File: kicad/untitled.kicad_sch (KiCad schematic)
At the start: 3 parts, among them J2 NMJ4HCD2, J3 AudioJack3_Dual_Switch, J4 Conn_01x03_Pin

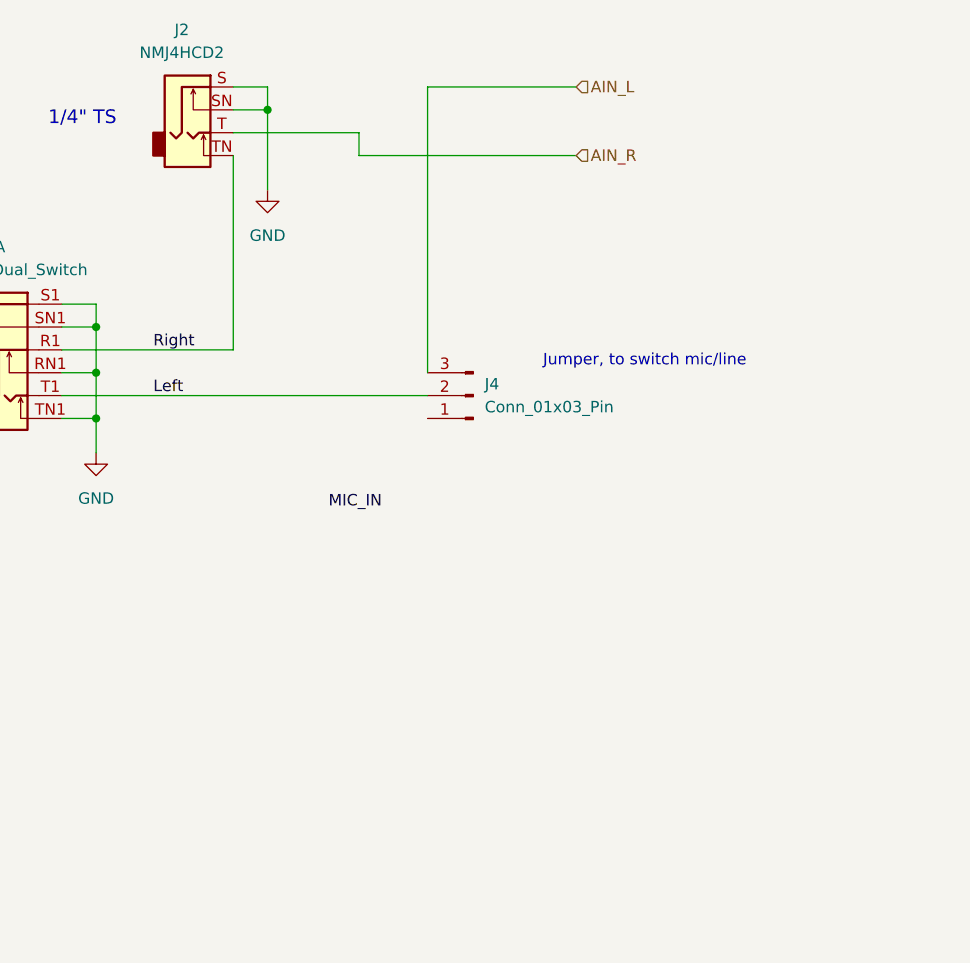
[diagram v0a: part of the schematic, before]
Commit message: microphone preamp. May give up on the jumper idea and add another jack
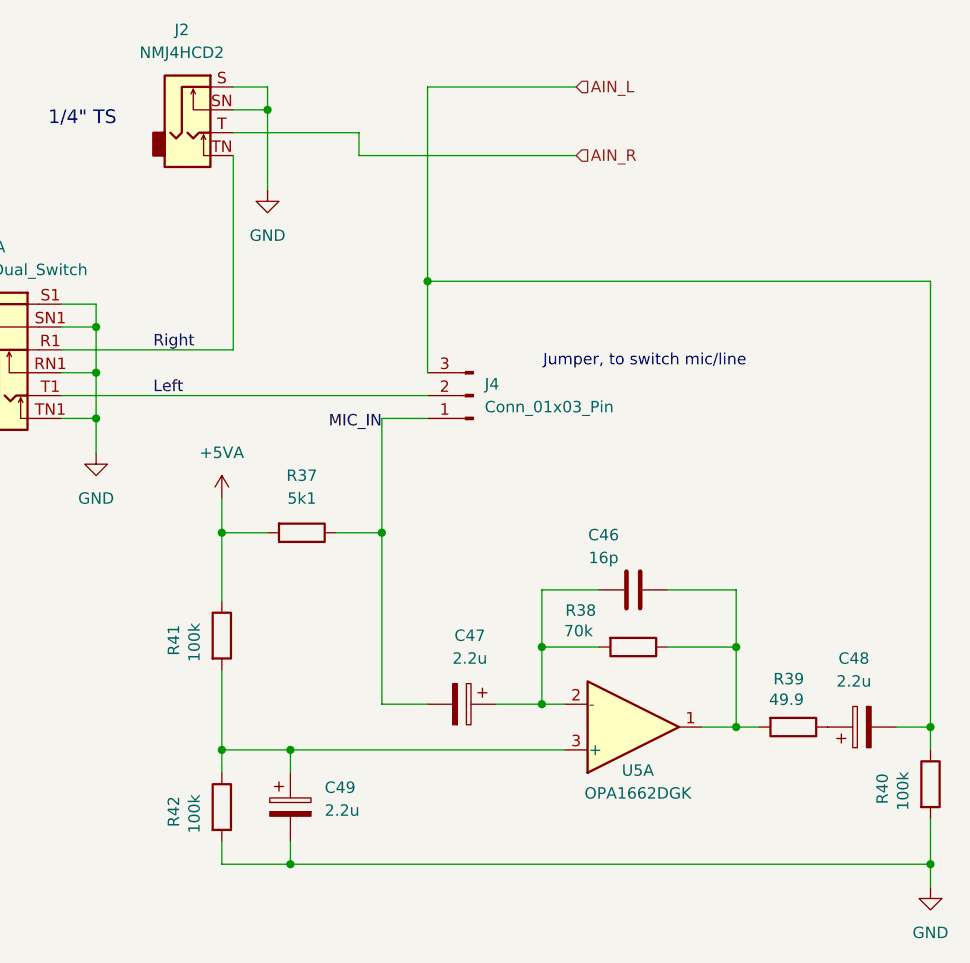
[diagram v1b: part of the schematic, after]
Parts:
- added C46: 16p, symbol Device:C
- added C47, C48, C49: 2.2u, symbol Device:C_Polarized
- added R37: 5k1, symbol Device:R
- added R38: 70k, symbol Device:R
- added R39: 49.9, symbol Device:R
- added R40, R41, R42: 100k, symbol Device:R
- added U5: OPA1662DGK, Package_SO:VSSOP-8_3x3mm_P0.65mm, symbol Amplifier_Operational:OPA1662DGK
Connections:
- net AIN_L: now also C48.2, R40.1
- net GND: now also C49.2, R40.2, R42.2
- net MIC_IN: now also J4.1 (Pin_1), C47.2, R37.1
- new net: C48.1, R39.1
- new net: C46.2, R38.1, R39.2, U5.1
- new net: C49.1, R41.2, R42.1, U5.3 (+)
- new net: C46.1, C47.1, R38.2, U5.2 (-)
- new net +5VA: R37.2, R41.1

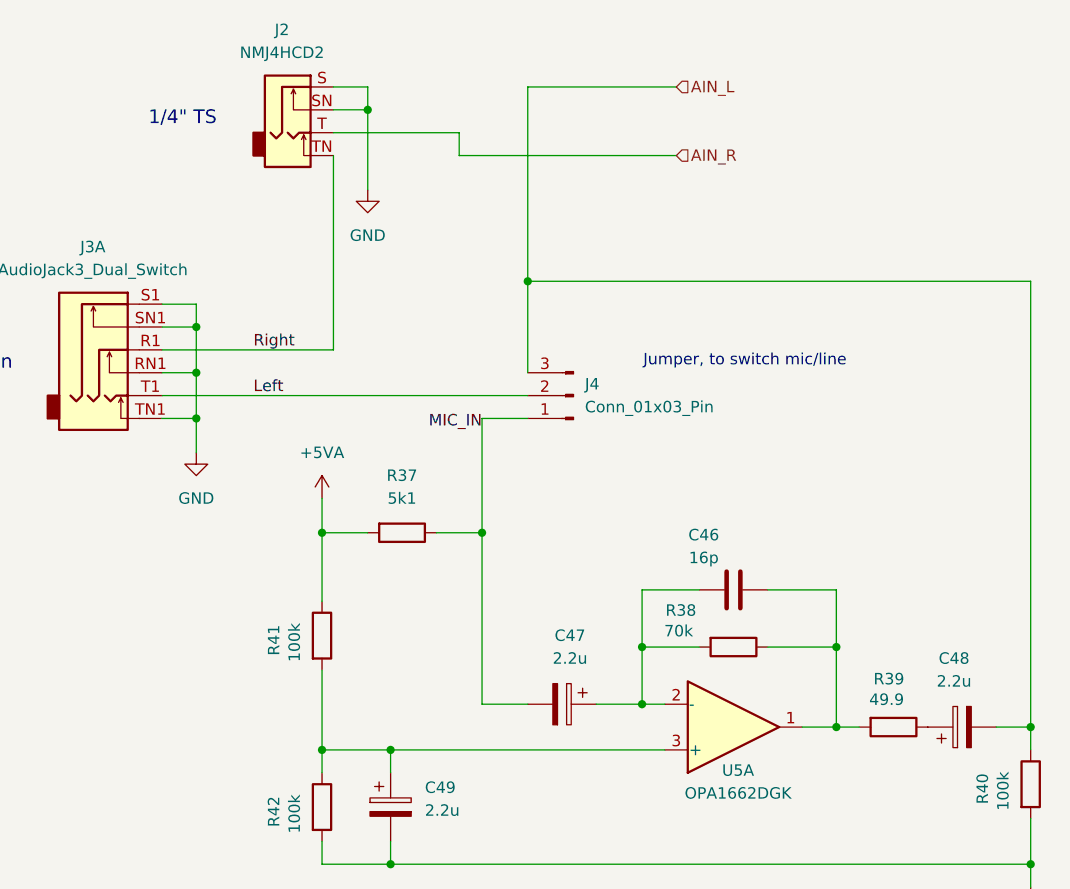
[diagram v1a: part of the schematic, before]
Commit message: DPDT switch for preamp toggle instead of jumper (not sure if this is a good solution)
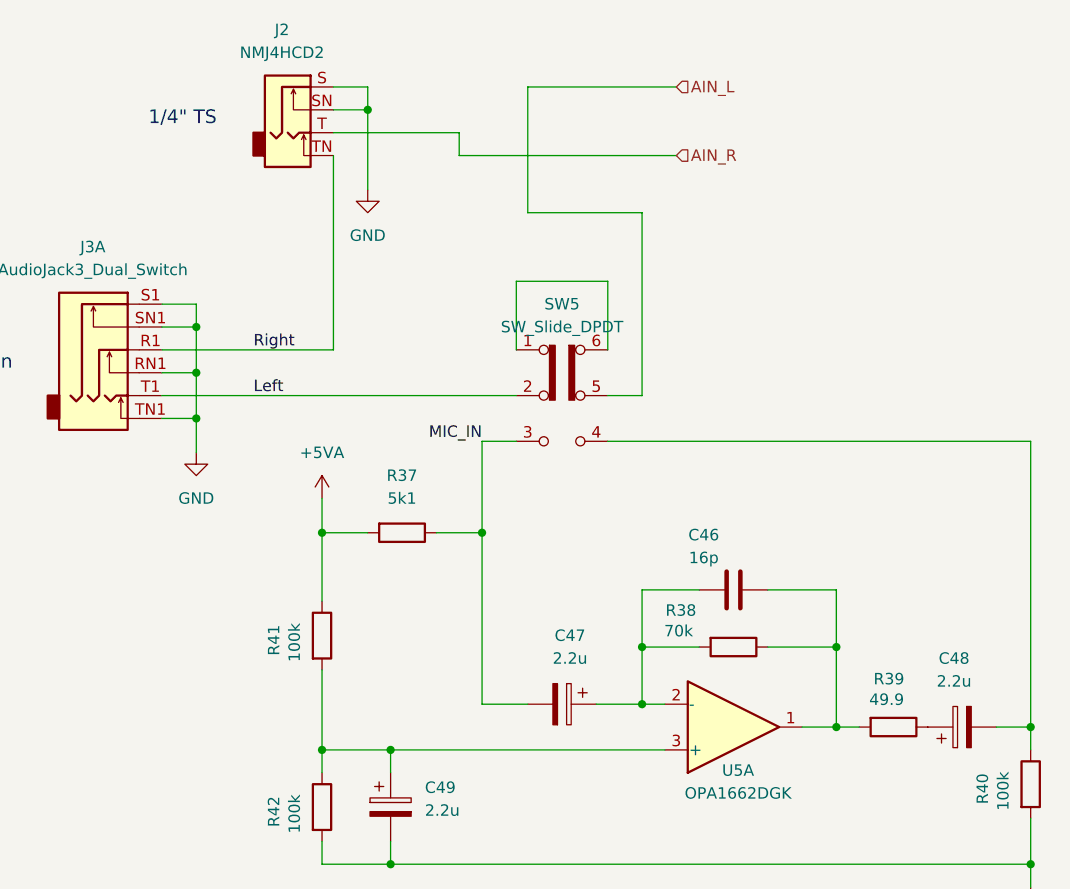
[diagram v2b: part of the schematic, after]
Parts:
- removed J4: Conn_01x03_Pin, symbol Connector:Conn_01x03_Pin
- added SW5: SW_Slide_DPDT, symbol Switch:SW_Slide_DPDT
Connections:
- net AIN_L: now also SW5.5 (B); no longer C48.2, R40.1
- net Left: now also SW5.2 (B)
- net MIC_IN: now also SW5.3 (C)
- new net: C48.2, R40.1, SW5.4 (A)
- new net: SW5.1 (A), SW5.6 (C)
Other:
- note removed: "Jumper, to switch mic/line"
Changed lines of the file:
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@@
-		)
-	)
-	(text "Jumper, to switch mic/line"
-		(exclude_from_sim no)
-		(at 120.65 106.68 0)
-		(effects
-			(font
-				(size 1.27 1.27)
-			)
 		)
 	)
@@
 	)
 	(junction
-		(at 152.4 147.32)
-		(diameter 0)
-		(color 0 0 0 0)
-	)
-	(junction
 		(at 109.22 144.78)
 		(diameter 0)
@@
 	)
 	(junction
-		(at 91.44 125.73)
+		(at 152.4 162.56)
 		(diameter 0)
 		(color 0 0 0 0)
 	)
 	(junction
-		(at 152.4 162.56)
+		(at 91.44 125.73)
 		(diameter 0)
 		(color 0 0 0 0)
@@
 	)
 	(junction
-		(at 96.52 97.79)
+		(at 152.4 147.32)
 		(diameter 0)
 		(color 0 0 0 0)
@@
 	(wire
 		(pts
+			(xy 95.25 105.41) (xy 95.25 97.79)
+		)
+		(stroke
+			(width 0)
+			(type default)
+		)
+	)
+	(wire
+		(pts
 			(xy 81.28 149.86) (xy 111.76 149.86)
 		)
@@
 	(wire
 		(pts
-			(xy 55.88 110.49) (xy 96.52 110.49)
+			(xy 95.25 115.57) (xy 91.44 115.57)
 		)
 		(stroke
@@
 	(wire
 		(pts
-			(xy 91.44 113.03) (xy 91.44 125.73)
-		)
-		(stroke
-			(width 0)
-			(type default)
-		)
-	)
-	(wire
-		(pts
 			(xy 73.66 162.56) (xy 73.66 160.02)
 		)
@@
 	(wire
 		(pts
+			(xy 109.22 90.17) (xy 96.52 90.17)
+		)
+		(stroke
+			(width 0)
+			(type default)
+		)
+	)
+	(wire
+		(pts
 			(xy 104.14 144.78) (xy 109.22 144.78)
 		)
@@
 	(wire
 		(pts
+			(xy 91.44 115.57) (xy 91.44 125.73)
+		)
+		(stroke
+			(width 0)
+			(type default)
+		)
+	)
+	(wire
+		(pts
 			(xy 74.93 76.2) (xy 78.74 76.2)
 		)
@@
 	(wire
 		(pts
+			(xy 105.41 110.49) (xy 109.22 110.49)
+		)
+		(stroke
+			(width 0)
+			(type default)
+		)
+	)
+	(wire
+		(pts
 			(xy 115.57 132.08) (xy 109.22 132.08)
 		)
@@
 	(wire
 		(pts
+			(xy 95.25 97.79) (xy 105.41 97.79)
+		)
+		(stroke
+			(width 0)
+			(type default)
+		)
+	)
+	(wire
+		(pts
 			(xy 55.88 100.33) (xy 59.69 100.33)
 		)
@@
 	(wire
 		(pts
+			(xy 152.4 115.57) (xy 152.4 147.32)
+		)
+		(stroke
+			(width 0)
+			(type default)
+		)
+	)
+	(wire
+		(pts
+			(xy 109.22 110.49) (xy 109.22 90.17)
+		)
+		(stroke
+			(width 0)
+			(type default)
+		)
+	)
+	(wire
+		(pts
 			(xy 59.69 113.03) (xy 59.69 116.84)
 		)
@@
 	(wire
 		(pts
-			(xy 96.52 97.79) (xy 152.4 97.79)
-		)
-		(stroke
-			(width 0)
-			(type default)
-		)
-	)
-	(wire
-		(pts
-			(xy 96.52 97.79) (xy 96.52 76.2)
+			(xy 96.52 90.17) (xy 96.52 76.2)
+		)
+		(stroke
+			(width 0)
+			(type default)
+		)
+	)
+	(wire
+		(pts
+			(xy 105.41 97.79) (xy 105.41 105.41)
 		)
 		(stroke
@@
 	(wire
 		(pts
-			(xy 96.52 107.95) (xy 96.52 97.79)
-		)
-		(stroke
-			(width 0)
-			(type default)
-		)
-	)
-	(wire
-		(pts
 			(xy 152.4 147.32) (xy 152.4 149.86)
 		)
@@
 	(wire
 		(pts
+			(xy 55.88 110.49) (xy 95.25 110.49)
+		)
+		(stroke
+			(width 0)
+			(type default)
+		)
+	)
+	(wire
+		(pts
 			(xy 148.59 147.32) (xy 152.4 147.32)
 		)
@@
 	(wire
 		(pts
+			(xy 105.41 115.57) (xy 152.4 115.57)
+		)
+		(stroke
+			(width 0)
+			(type default)
+		)
+	)
+	(wire
+		(pts
 			(xy 73.66 162.56) (xy 81.28 162.56)
 		)
@@
 	(wire
 		(pts
-			(xy 152.4 147.32) (xy 152.4 97.79)
-		)
-		(stroke
-			(width 0)
-			(type default)
-		)
-	)
-	(wire
-		(pts
 			(xy 130.81 147.32) (xy 133.35 147.32)
 		)
@@
 		(pts
 			(xy 109.22 138.43) (xy 109.22 144.78)
-		)
-		(stroke
-			(width 0)
-			(type default)
-		)
-	)
-	(wire
-		(pts
-			(xy 96.52 113.03) (xy 91.44 113.03)
 		)
 		(stroke
@@
 	)
 	(label "MIC_IN"
-		(at 91.44 114.3 180)
+		(at 91.44 115.57 180)
 		(effects
 			(font
@@
 	)
 	(symbol
+		(lib_id "Switch:SW_Slide_DPDT")
+		(at 100.33 110.49 0)
+		(unit 1)
+		(body_style 1)
+		(exclude_from_sim no)
+		(in_bom yes)
+		(on_board yes)
+		(in_pos_files yes)
+		(dnp no)
+		(fields_autoplaced yes)
+		(property "Reference" "SW5"
+			(at 100.33 100.33 0)
+			(show_name no)
+			(do_not_autoplace no)
+			(effects
+				(font
+					(size 1.27 1.27)
+				)
+			)
+		)
+		(property "Value" "SW_Slide_DPDT"
+			(at 100.33 102.87 0)
+			(show_name no)
+			(do_not_autoplace no)
+			(effects
+				(font
+					(size 1.27 1.27)
+				)
+			)
+		)
+		(property "Footprint" ""
+			(at 114.3 105.41 0)
+			(hide yes)
+			(show_name no)
+			(do_not_autoplace no)
+			(effects
+				(font
+					(size 1.27 1.27)
+				)
+			)
+		)
+		(property "Datasheet" ""
+			(at 100.33 110.49 0)
+			(hide yes)
+			(show_name no)
+			(do_not_autoplace no)
+			(effects
+				(font
+					(size 1.27 1.27)
+				)
+			)
+		)
+		(property "Description" "Slide Switch, dual pole double throw"
+			(at 100.33 110.49 0)
+			(hide yes)
+			(show_name no)
+			(do_not_autoplace no)
+			(effects
+				(font
+					(size 1.27 1.27)
+				)
+			)
+		)
+		(pin "4"
+		)
+		(pin "6"
+		)
+		(pin "5"
+		)
+		(pin "2"
+		)
+		(pin "3"
+		)
+		(pin "1"
+		)
+		(instances
+			(project "first"
+				(path "/580becc7-fa47-4b4d-a43e-4b9316967eb7/7adb74f9-e933-4ca7-8fff-913837d4ebb7"
+					(reference "SW5")
+					(unit 1)
+				)
+			)
+		)
+	)
+	(symbol
 		(lib_id "power:+5VA")
 		(at 73.66 121.92 0)
@@
 					(unit 1)
 				)
-			)
-		)
-	)
-	(symbol
-		(lib_id "Connector:Conn_01x03_Pin")
-		(at 101.6 110.49 180)
-		(unit 1)
-		(body_style 1)
-		(exclude_from_sim no)
-		(in_bom yes)
-		(on_board yes)
-		(in_pos_files yes)
-		(dnp no)
-		(fields_autoplaced yes)
-		(property "Reference" "J4"
-			(at 102.87 109.2199 0)
-			(show_name no)
-			(do_not_autoplace no)
-			(effects
-				(font
-					(size 1.27 1.27)
-				)
-				(justify right)
-			)
-		)
-		(property "Value" "Conn_01x03_Pin"
-			(at 102.87 111.7599 0)
-			(show_name no)
-			(do_not_autoplace no)
-			(effects
-				(font
-					(size 1.27 1.27)
-				)
-				(justify right)
-			)
-		)
-		(property "Footprint" ""
-			(at 101.6 110.49 0)
-			(hide yes)
-			(show_name no)
-			(do_not_autoplace no)
-			(effects
-				(font
-					(size 1.27 1.27)
-				)
-			)
-		)
-		(property "Datasheet" ""
-			(at 101.6 110.49 0)
-			(hide yes)
-			(show_name no)
-			(do_not_autoplace no)
-			(effects
-				(font
-					(size 1.27 1.27)
-				)
-			)
-		)
-		(property "Description" "Generic connector, single row, 01x03, script generated"
-			(at 101.6 110.49 0)
-			(hide yes)
-			(show_name no)
-			(do_not_autoplace no)
-			(effects
-				(font
-					(size 1.27 1.27)
-				)
-			)
-		)
-		(pin "2"
-		)
-		(pin "3"
-		)
-		(pin "1"
-		)
-		(instances
-			(project "first"
-				(path "/580becc7-fa47-4b4d-a43e-4b9316967eb7/7adb74f9-e933-4ca7-8fff-913837d4ebb7"
-					(reference "J4")
-					(unit 1)
-				)

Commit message: decoupling cleanup, new LDO, I2C pullups
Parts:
- renumbered C47 to C40, C46 to C41, C48 to C42, C49 to C43
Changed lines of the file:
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@@
 		(dnp no)
 		(fields_autoplaced yes)
-		(property "Reference" "C49"
+		(property "Reference" "C43"
 			(at 85.09 154.0509 0)
 			(show_name no)
@@
 			(project "first"
 				(path "/580becc7-fa47-4b4d-a43e-4b9316967eb7/7adb74f9-e933-4ca7-8fff-913837d4ebb7"
-					(reference "C49")
+					(reference "C43")
 					(unit 1)
 				)
@@
 		(dnp no)
 		(fields_autoplaced yes)
-		(property "Reference" "C47"
+		(property "Reference" "C40"
 			(at 101.219 137.16 90)
 			(show_name no)
@@
 			(project "first"
 				(path "/580becc7-fa47-4b4d-a43e-4b9316967eb7/7adb74f9-e933-4ca7-8fff-913837d4ebb7"
-					(reference "C47")
+					(reference "C40")
 					(unit 1)
 				)
@@
 		(dnp no)
 		(fields_autoplaced yes)
-		(property "Reference" "C48"
+		(property "Reference" "C42"
 			(at 143.891 139.7 90)
 			(show_name no)
@@
 			(project "first"
 				(path "/580becc7-fa47-4b4d-a43e-4b9316967eb7/7adb74f9-e933-4ca7-8fff-913837d4ebb7"
-					(reference "C48")
+					(reference "C42")
 					(unit 1)
 				)
@@
 		(in_pos_files yes)
 		(dnp no)
-		(property "Reference" "C46"
+		(property "Reference" "C41"
 			(at 116.078 125.984 90)
 			(show_name no)
@@
 			(project "first"
 				(path "/580becc7-fa47-4b4d-a43e-4b9316967eb7/7adb74f9-e933-4ca7-8fff-913837d4ebb7"
-					(reference "C46")
-					(unit 1)
-				)
+					(reference "C41")
+					(unit 1)
+				)

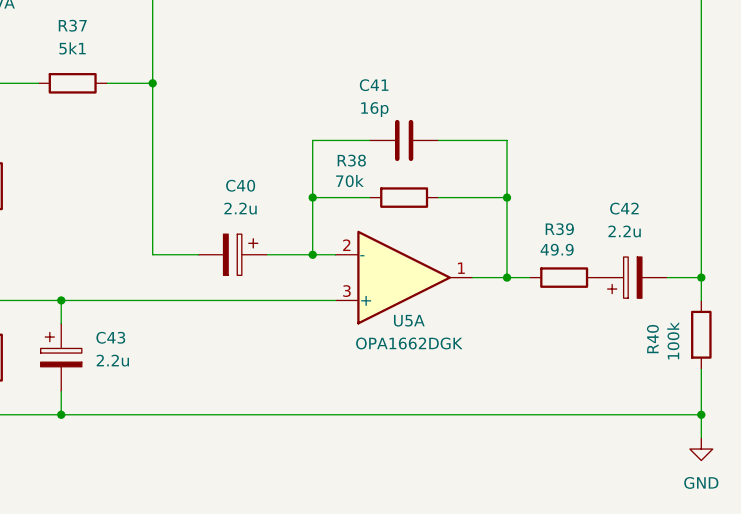
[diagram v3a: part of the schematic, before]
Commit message: opa1662->opa1678, one less package
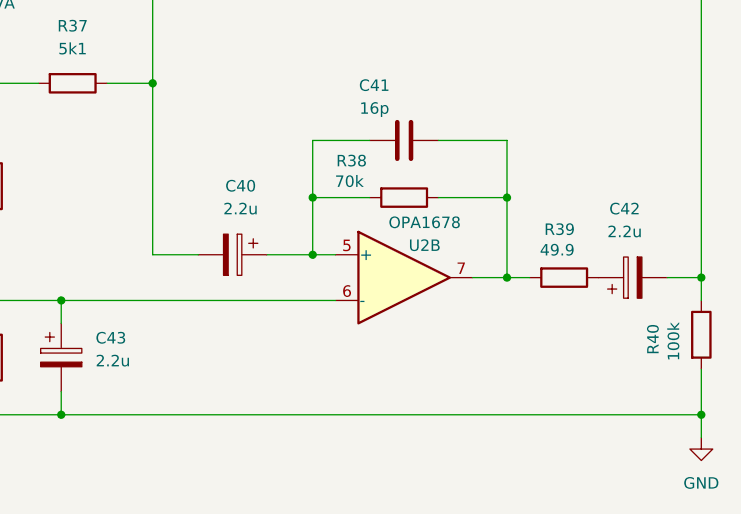
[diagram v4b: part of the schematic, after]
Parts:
- removed U5: OPA1662DGK, Package_SO:VSSOP-8_3x3mm_P0.65mm, symbol Amplifier_Operational:OPA1662DGK
- added U2: OPA1678, Package_SO:SOIC-8_3.9x4.9mm_P1.27mm, symbol Amplifier_Operational:NE5532
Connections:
- net at C41.2, R38.1, R39.2: now also U2.7
- net at C43.1, R41.2, R42.1: now also U2.6 (-)
- net at C40.1, C41.1, R38.2: now also U2.5 (+)
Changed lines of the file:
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@@
+	)
+	(symbol
+		(lib_id "Amplifier_Operational:NE5532")
+		(at 119.38 147.32 0)
+		(unit 2)
+		(body_style 1)
+		(exclude_from_sim no)
+		(in_bom yes)
+		(on_board yes)
+		(in_pos_files yes)
+		(dnp no)
+		(property "Reference" "U2"
+			(at 121.666 143.764 0)
+			(show_name no)
+			(do_not_autoplace no)
+			(effects
+				(font
+					(size 1.27 1.27)
+				)
+			)
+		)
+		(property "Value" "OPA1678"
+			(at 121.666 141.224 0)
+			(show_name no)
+			(do_not_autoplace no)
+			(effects
+				(font
+					(size 1.27 1.27)
+				)
+			)
+		)
+		(property "Footprint" "Package_SO:SOIC-8_3.9x4.9mm_P1.27mm"
+			(at 119.38 147.32 0)
+			(hide yes)
+			(show_name no)
+			(do_not_autoplace no)
+			(effects
+				(font
+					(size 1.27 1.27)
+				)
+			)
+		)
+		(property "Datasheet" "http://www.ti.com/lit/ds/symlink/ne5532.pdf"
+			(at 119.38 147.32 0)
+			(hide yes)
+			(show_name no)
+			(do_not_autoplace no)
+			(effects
+				(font
+					(size 1.27 1.27)
+				)
+			)
+		)
+		(property "Description" "Dual Low-Noise Operational Amplifiers, DIP-8/SOIC-8"
+			(at 119.38 147.32 0)
+			(hide yes)
+			(show_name no)
+			(do_not_autoplace no)
+			(effects
+				(font
+					(size 1.27 1.27)
+				)
+			)
+		)
+		(pin "6"
+		)
+		(pin "8"
+		)
+		(pin "5"
+		)
+		(pin "1"
+		)
+		(pin "4"
+		)
+		(pin "3"
+		)
+		(pin "7"
+		)
+		(pin "2"
+		)
+		(instances
+			(project "first"
+				(path "/580becc7-fa47-4b4d-a43e-4b9316967eb7/7adb74f9-e933-4ca7-8fff-913837d4ebb7"
+					(reference "U2")
+					(unit 2)
+				)
+			)
+		)
 	)
 	(symbol
@@
 					(unit 1)
 				)
-			)
-		)
-	)
-	(symbol
-		(lib_id "Amplifier_Operational:OPA1662DGK")
-		(at 119.38 147.32 0)
-		(mirror x)
-		(unit 1)
-		(body_style 1)
-		(exclude_from_sim no)
-		(in_bom yes)
-		(on_board yes)
-		(in_pos_files yes)
-		(dnp no)
-		(property "Reference" "U5"
-			(at 119.888 152.146 0)
-			(show_name no)
-			(do_not_autoplace no)
-			(effects
-				(font
-					(size 1.27 1.27)
-				)
-			)
-		)
-		(property "Value" "OPA1662DGK"
-			(at 119.888 154.686 0)
-			(show_name no)
-			(do_not_autoplace no)
-			(effects
-				(font
-					(size 1.27 1.27)
-				)
-			)
-		)
-		(property "Footprint" "Package_SO:VSSOP-8_3x3mm_P0.65mm"
-			(at 119.38 147.32 0)
-			(hide yes)
-			(show_name no)
-			(do_not_autoplace no)
-			(effects
-				(font
-					(size 1.27 1.27)
-				)
-			)
-		)
-		(property "Datasheet" "https://www.ti.com/lit/ds/symlink/opa1662.pdf"
-			(at 119.38 147.32 0)
-			(hide yes)
-			(show_name no)
-			(do_not_autoplace no)
-			(effects
-				(font
-					(size 1.27 1.27)
-				)
-			)
-		)
-		(property "Description" "Dual Low-Power, Low-Noise, Low-Distortion, Bipolar-Input SoundPlus Audio Operational Amplifiers, VSSOP-8"
-			(at 119.38 147.32 0)
-			(hide yes)
-			(show_name no)
-			(do_not_autoplace no)
-			(effects
-				(font
-					(size 1.27 1.27)
-				)
-			)
-		)
-		(pin "4"
-		)
-		(pin "2"
-		)
-		(pin "7"
-		)
-		(pin "3"
-		)
-		(pin "8"
-		)
-		(pin "6"
-		)
-		(pin "5"
-		)
-		(pin "1"
-		)
-		(instances
-			(project "first"
-				(path "/580becc7-fa47-4b4d-a43e-4b9316967eb7/7adb74f9-e933-4ca7-8fff-913837d4ebb7"
-					(reference "U5")
-					(unit 1)
-				)
